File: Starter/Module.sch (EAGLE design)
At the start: 3 parts

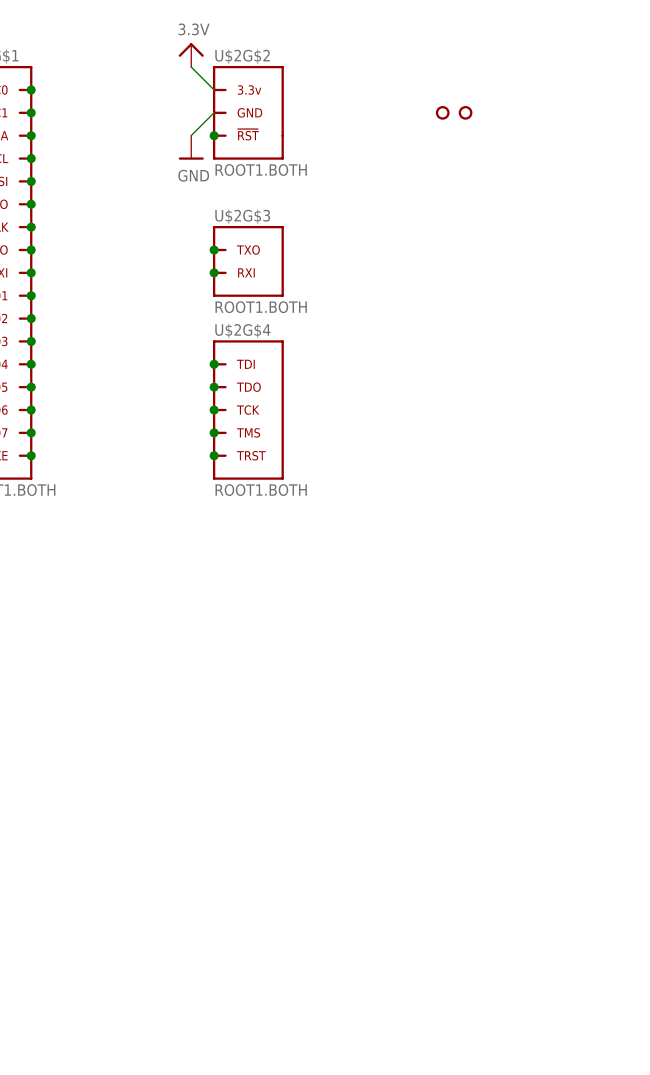
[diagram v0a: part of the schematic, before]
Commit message: Updated Starter Module for updated holes, support for external power, and updated header from library.
Signed-off-by: Cruz Monrreal II <Cruz.Monrreal@gmail.com>
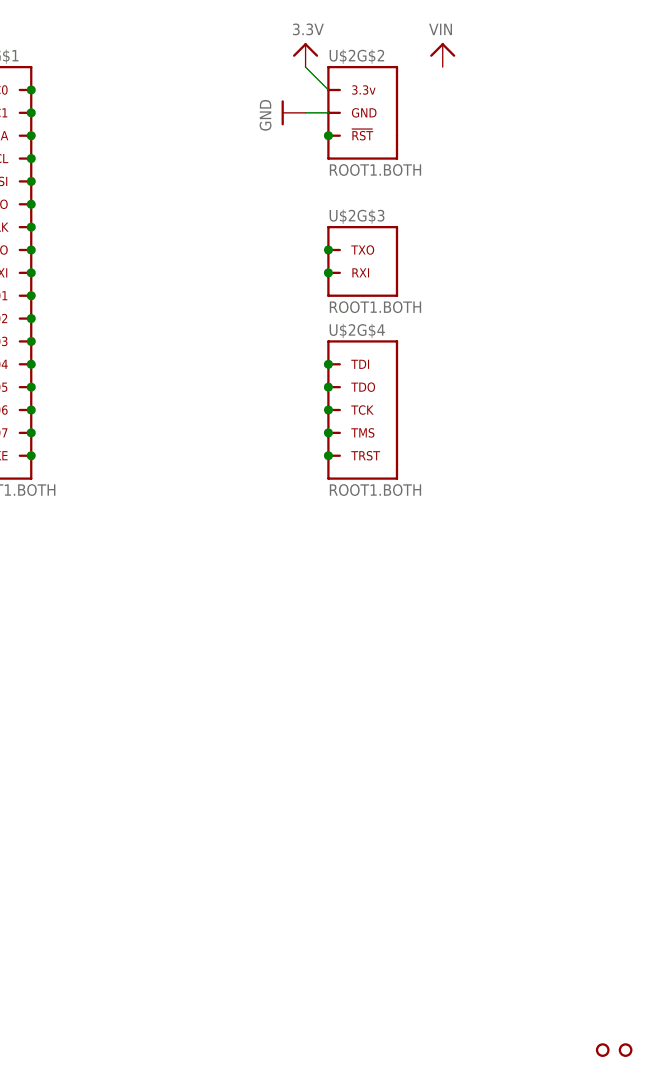
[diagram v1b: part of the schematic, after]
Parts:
- U$3, U$4: value HOLE.2MM -> HOLE.#2; device .screw_holes:HOLE.2MM -> .screw_holes:HOLE.#2
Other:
- moved on the sheet: U$2G$2, U$2G$3, U$2G$4
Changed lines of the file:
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@@
 <?xml version="1.0" encoding="utf-8"?>
 <!DOCTYPE eagle SYSTEM "eagle.dtd">
-<eagle version="6.1">
+<eagle version="6.3">
 <drawing>
 <settings>
@@
 <grid distance="0.1" unitdist="inch" unit="inch" style="lines" multiple="1" display="no" altdistance="0.01" altunitdist="inch" altunit="inch"/>
 <layers>
-<layer number="1" name="Top" color="4" fill="1" visible="yes" active="no"/>
-<layer number="16" name="Bottom" color="1" fill="1" visible="yes" active="no"/>
-<layer number="17" name="Pads" color="2" fill="1" visible="yes" active="no"/>
-<layer number="18" name="Vias" color="2" fill="1" visible="yes" active="no"/>
-<layer number="19" name="Unrouted" color="6" fill="1" visible="yes" active="no"/>
-<layer number="20" name="Dimension" color="15" fill="1" visible="yes" active="no"/>
-<layer number="21" name="tPlace" color="7" fill="1" visible="yes" active="no"/>
-<layer number="22" name="bPlace" color="7" fill="1" visible="yes" active="no"/>
-<layer number="23" name="tOrigins" color="15" fill="1" visible="yes" active="no"/>
-<layer number="24" name="bOrigins" color="15" fill="1" visible="yes" active="no"/>
-<layer number="25" name="tNames" color="7" fill="1" visible="yes" active="no"/>
-<layer number="26" name="bNames" color="7" fill="1" visible="yes" active="no"/>
-<layer number="27" name="tValues" color="7" fill="1" visible="yes" active="no"/>
-<layer number="28" name="bValues" color="7" fill="1" visible="yes" active="no"/>
+<layer number="1" name="Top" color="4" fill="1" visible="no" active="no"/>
+<layer number="2" name="Route2" color="1" fill="3" visible="no" active="no"/>
+<layer number="3" name="Route3" color="4" fill="3" visible="no" active="no"/>
+<layer number="4" name="Route4" color="1" fill="4" visible="no" active="no"/>
+<layer number="5" name="Route5" color="4" fill="4" visible="no" active="no"/>
+<layer number="6" name="Route6" color="1" fill="8" visible="no" active="no"/>
+<layer number="7" name="Route7" color="4" fill="8" visible="no" active="no"/>
+<layer number="8" name="Route8" color="1" fill="2" visible="no" active="no"/>
+<layer number="9" name="Route9" color="4" fill="2" visible="no" active="no"/>
+<layer number="10" name="Route10" color="1" fill="7" visible="no" active="no"/>
+<layer number="11" name="Route11" color="4" fill="7" visible="no" active="no"/>
+<layer number="12" name="Route12" color="1" fill="5" visible="no" active="no"/>
+<layer number="13" name="Route13" color="4" fill="5" visible="no" active="no"/>
+<layer number="14" name="Route14" color="1" fill="6" visible="no" active="no"/>
+<layer number="15" name="Route15" color="4" fill="6" visible="no" active="no"/>
+<layer number="16" name="Bottom" color="1" fill="1" visible="no" active="no"/>
+<layer number="17" name="Pads" color="2" fill="1" visible="no" active="no"/>
+<layer number="18" name="Vias" color="2" fill="1" visible="no" active="no"/>
+<layer number="19" name="Unrouted" color="6" fill="1" visible="no" active="no"/>
+<layer number="20" name="Dimension" color="15" fill="1" visible="no" active="no"/>
+<layer number="21" name="tPlace" color="7" fill="1" visible="no" active="no"/>
+<layer number="22" name="bPlace" color="7" fill="1" visible="no" active="no"/>
+<layer number="23" name="tOrigins" color="15" fill="1" visible="no" active="no"/>
+<layer number="24" name="bOrigins" color="15" fill="1" visible="no" active="no"/>
+<layer number="25" name="tNames" color="7" fill="1" visible="no" active="no"/>
+<layer number="26" name="bNames" color="7" fill="1" visible="no" active="no"/>
+<layer number="27" name="tValues" color="7" fill="1" visible="no" active="no"/>
+<layer number="28" name="bValues" color="7" fill="1" visible="no" active="no"/>
 <layer number="29" name="tStop" color="7" fill="3" visible="no" active="no"/>
 <layer number="30" name="bStop" color="7" fill="6" visible="no" active="no"/>
@@
 <layer number="35" name="tGlue" color="7" fill="4" visible="no" active="no"/>
 <layer number="36" name="bGlue" color="7" fill="5" visible="no" active="no"/>
-<layer number="37" name="tTest" color="7" fill="1" visible="yes" active="no"/>
-<layer number="38" name="bTest" color="7" fill="1" visible="yes" active="no"/>
+<layer number="37" name="tTest" color="7" fill="1" visible="no" active="no"/>
+<layer number="38" name="bTest" color="7" fill="1" visible="no" active="no"/>
 <layer number="39" name="tKeepout" color="4" fill="11" visible="no" active="no"/>
 <layer number="40" name="bKeepout" color="1" fill="11" visible="no" active="no"/>
@@
 <layer number="44" name="Drills" color="7" fill="1" visible="no" active="no"/>
 <layer number="45" name="Holes" color="7" fill="1" visible="no" active="no"/>
-<layer number="46" name="Milling" color="3" fill="1" visible="yes" active="no"/>
-<layer number="47" name="Measures" color="7" fill="1" visible="yes" active="no"/>
-<layer number="48" name="Document" color="7" fill="1" visible="yes" active="no"/>
-<layer number="49" name="Reference" color="7" fill="1" visible="yes" active="no"/>
-<layer number="50" name="dxf" color="7" fill="1" visible="yes" active="no"/>
-<layer number="51" name="tDocu" color="7" fill="1" visible="yes" active="no"/>
-<layer number="52" name="bDocu" color="7" fill="1" visible="yes" active="no"/>
-<layer number="53" name="tGND_GNDA" color="7" fill="9" visible="yes" active="no"/>
-<layer number="54" name="bGND_GNDA" color="1" fill="9" visible="yes" active="no"/>
-<layer number="56" name="wert" color="7" fill="1" visible="yes" active="no"/>
+<layer number="46" name="Milling" color="3" fill="1" visible="no" active="no"/>
+<layer number="47" name="Measures" color="7" fill="1" visible="no" active="no"/>
+<layer number="48" name="Document" color="7" fill="1" visible="no" active="no"/>
+<layer number="49" name="Reference" color="7" fill="1" visible="no" active="no"/>
+<layer number="50" name="dxf" color="7" fill="1" visible="no" active="no"/>
+<layer number="51" name="tDocu" color="7" fill="1" visible="no" active="no"/>
+<layer number="52" name="bDocu" color="7" fill="1" visible="no" active="no"/>
+<layer number="53" name="tGND_GNDA" color="7" fill="9" visible="no" active="no"/>
+<layer number="54" name="bGND_GNDA" color="1" fill="9" visible="no" active="no"/>
+<layer number="56" name="wert" color="7" fill="1" visible="no" active="no"/>
 <layer number="91" name="Nets" color="2" fill="1" visible="yes" active="yes"/>
 <layer number="92" name="Busses" color="1" fill="1" visible="yes" active="yes"/>
@@
 <parts>
 <part name="U$1" library="thinkmaketest" deviceset="A4_LAYOUT" device=""/>
-<part name="U$4" library=".screw_holes" deviceset="HOLE" device=".2MM"/>
+<part name="U$4" library=".screw_holes" deviceset="HOLE" device=".#2" value="HOLE.#2"/>
 <part name="U$5" library="microbuilder" deviceset="GND" device=""/>
 <part name="U$6" library="microbuilder" deviceset="3.3V" device=""/>
-<part name="U$3" library=".screw_holes" deviceset="HOLE" device=".2MM"/>
+<part name="U$3" library=".screw_holes" deviceset="HOLE" device=".#2" value="HOLE.#2"/>
 <part name="U$2" library="thinkmaketest" deviceset="ROOT1" device=".BOTH"/>
+<part name="U$7" library="microbuilder" deviceset="VIN" device=""/>
 </parts>
 <sheets>
@@
 <instances>
 <instance part="U$1" gate="G$1" x="0" y="0"/>
-<instance part="U$4" gate="G$1" x="231.14" y="127"/>
-<instance part="U$5" gate="G$1" x="203.2" y="121.92"/>
-<instance part="U$6" gate="G$1" x="203.2" y="132.08"/>
-<instance part="U$3" gate="G$1" x="233.68" y="127"/>
+<instance part="U$4" gate="G$1" x="248.92" y="22.86"/>
+<instance part="U$5" gate="G$1" x="213.36" y="127" rot="R270"/>
+<instance part="U$6" gate="G$1" x="215.9" y="132.08"/>
+<instance part="U$3" gate="G$1" x="251.46" y="22.86"/>
 <instance part="U$2" gate="G$1" x="182.88" y="111.76"/>
-<instance part="U$2" gate="G$2" x="205.74" y="127"/>
-<instance part="U$2" gate="G$3" x="208.28" y="109.22"/>
-<instance part="U$2" gate="G$4" x="208.28" y="93.98"/>
+<instance part="U$2" gate="G$2" x="218.44" y="127"/>
+<instance part="U$2" gate="G$3" x="220.98" y="109.22"/>
+<instance part="U$2" gate="G$4" x="220.98" y="93.98"/>
+<instance part="U$7" gate="G$1" x="231.14" y="134.62"/>
 </instances>
 <busses>
@@
 <segment>
 <pinref part="U$5" gate="G$1" pin="GND"/>
-<wire x1="203.2" y1="124.46" x2="205.74" y2="127" width="0.1524" layer="91"/>
+<wire x1="215.9" y1="127" x2="218.44" y2="127" width="0.1524" layer="91"/>
 <pinref part="U$2" gate="G$2" pin="GND"/>
 </segment>
@@
 <segment>
 <pinref part="U$6" gate="G$1" pin="3.3V"/>
-<wire x1="205.74" y1="129.54" x2="203.2" y2="132.08" width="0.1524" layer="91"/>
+<wire x1="218.44" y1="129.54" x2="215.9" y2="132.08" width="0.1524" layer="91"/>
 <pinref part="U$2" gate="G$2" pin="3.3V"/>
 </segment>
@@
 <segment>
 <pinref part="U$2" gate="G$4" pin="TDI"/>
-<junction x="205.74" y="99.06"/>
+<junction x="218.44" y="99.06"/>
 </segment>
 </net>
@@
 <segment>
 <pinref part="U$2" gate="G$4" pin="TDO"/>
-<junction x="205.74" y="96.52"/>
+<junction x="218.44" y="96.52"/>
 </segment>
 </net>
@@
 <segment>
 <pinref part="U$2" gate="G$4" pin="TCK"/>
-<junction x="205.74" y="93.98"/>
+<junction x="218.44" y="93.98"/>
 </segment>
 </net>
@@
 <segment>
 <pinref part="U$2" gate="G$4" pin="TMS"/>
-<junction x="205.74" y="91.44"/>
+<junction x="218.44" y="91.44"/>
 </segment>
 </net>
@@
 <segment>
 <pinref part="U$2" gate="G$4" pin="TRST"/>
-<junction x="205.74" y="88.9"/>
+<junction x="218.44" y="88.9"/>
 </segment>
 </net>
@@
 <segment>
 <pinref part="U$2" gate="G$3" pin="RXI"/>
-<junction x="205.74" y="109.22"/>
+<junction x="218.44" y="109.22"/>
 </segment>
 </net>
@@
 <segment>
 <pinref part="U$2" gate="G$3" pin="TXO"/>
-<junction x="205.74" y="111.76"/>
+<junction x="218.44" y="111.76"/>
 </segment>
 </net>
@@
 <segment>
 <pinref part="U$2" gate="G$2" pin="!RST"/>
-<junction x="205.74" y="124.46"/>
-</segment>
-</net>
+<junction x="218.44" y="124.46"/>
+</segment>
+</net>
